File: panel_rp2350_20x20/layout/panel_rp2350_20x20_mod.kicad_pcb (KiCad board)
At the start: 6 copper layers, 45 x 45 mm, 548 parts, among them J1 Conn_01x04, J2 Conn_01x05, J3 Conn_01x05, J4 Conn_01x05, J5 Conn_01x05, SW1 SW_Push, SW2 SW_Push, U1 APS6404L-3SQR, U10 UCC27517, U11 UCC27517, U12 UCC27517, U13 UCC27517, U14 UCC27517, U15 UCC27517, U16 UCC27517, U17 UCC27517, U18 UCC27517, U19 UCC27517, U2 RP2354B_80QFN, U20 UCC27517, U21 UCC27517, U22 UCC27517, U23 UCC27517, U24 UCC27517, U25 UCC27517, U26 UCC27517, U27 UCC27517, U28 UCC27517, U29 UCC27517, U3 UCC27517, U30 UCC27517, U31 UCC27517, U32 UCC27517, U33 UCC27517, U34 UCC27517, U35 UCC27517, U36 UCC27517, U37 UCC27517, U38 UCC27517, U39 UCC27517, U4 UCC27517, U40 UCC27517, U41 UCC27517, U42 UCC27517, U43 AP2112K-3.3, U5 UCC27517, U6 UCC27517, U7 UCC27517, U8 UCC27517, U9 UCC27517, Y1 ABM8-272-T3

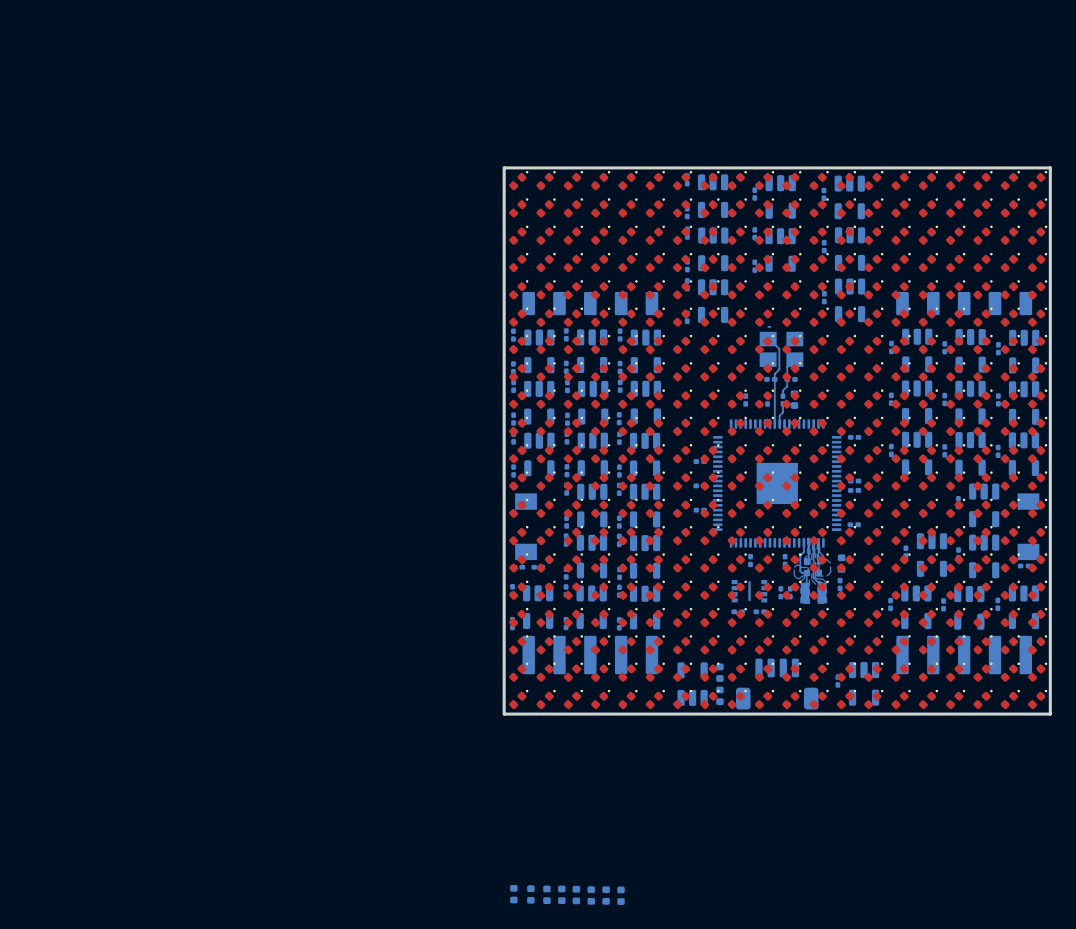
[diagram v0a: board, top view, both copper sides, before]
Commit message: More work on rp2350 20x20 panel.
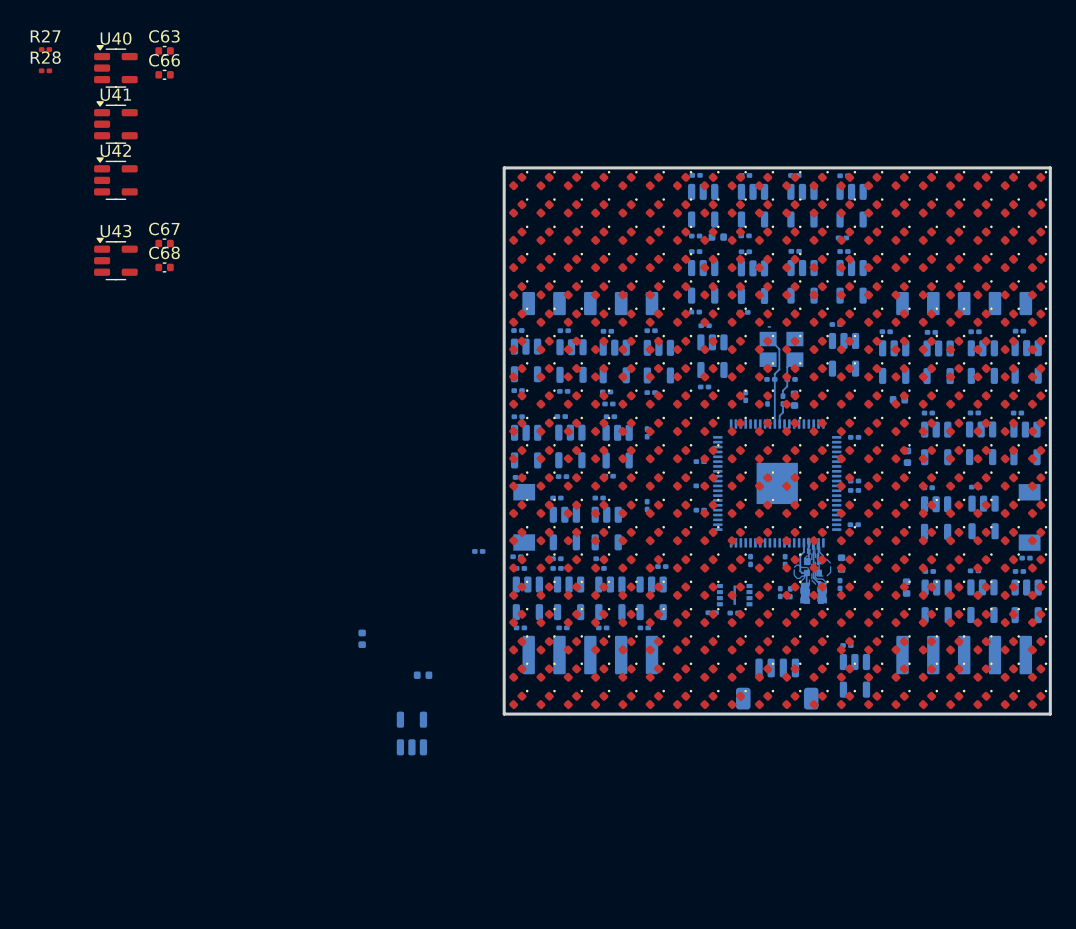
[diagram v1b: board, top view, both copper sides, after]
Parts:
- C63, C66, C67, C68, R27, R28, U40, U41, U42, U43: moved to F.Cu
- moved U40 83.2 mm to (18.0, 41.8), turned to 0 degrees
- moved C63 78.5 mm to (22.0, 40.4), turned to 0 degrees
- moved U41 77.0 mm to (18.0, 46.4), turned to 0 degrees
- moved U42 74.3 mm to (18.0, 51.0), turned to 0 degrees
- moved C66 74.0 mm to (22.0, 42.3), turned to 0 degrees
- moved R28 60.6 mm to (12.2, 42.0), turned to 0 degrees
- moved C67 59.0 mm to (22.0, 56.2), turned to 0 degrees
- moved U43 58.9 mm to (18.0, 57.6), turned to 0 degrees
- moved C68 56.6 mm to (22.0, 58.2), turned to 0 degrees
- moved C61 55.5 mm to (67.6, 55.7), turned to 180 degrees
- moved R27 54.6 mm to (12.2, 40.2), turned to 0 degrees
- moved U39 51.5 mm to (42.4, 96.6), turned to 90 degrees
- moved C59 50.0 mm to (82.5, 69.1), turned to 180 degrees
- moved C60 46.0 mm to (83.2, 73.8)
- moved C62 36.3 mm to (83.2, 84.6)
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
